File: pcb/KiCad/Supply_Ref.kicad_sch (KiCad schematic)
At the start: 39 parts, among them J9 RF_Shield_One_Piece, U1 LT3045EMSE, U2 LT3094EMSE, U3 LT1236-10, U6 LT8610

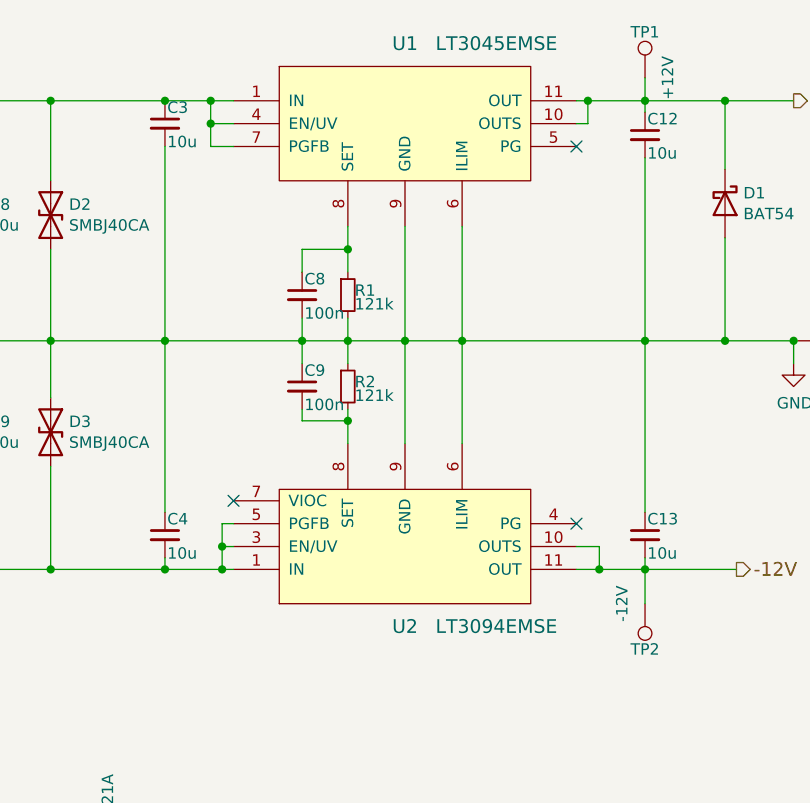
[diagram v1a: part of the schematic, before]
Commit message: Fix custom symbols. Update production files.
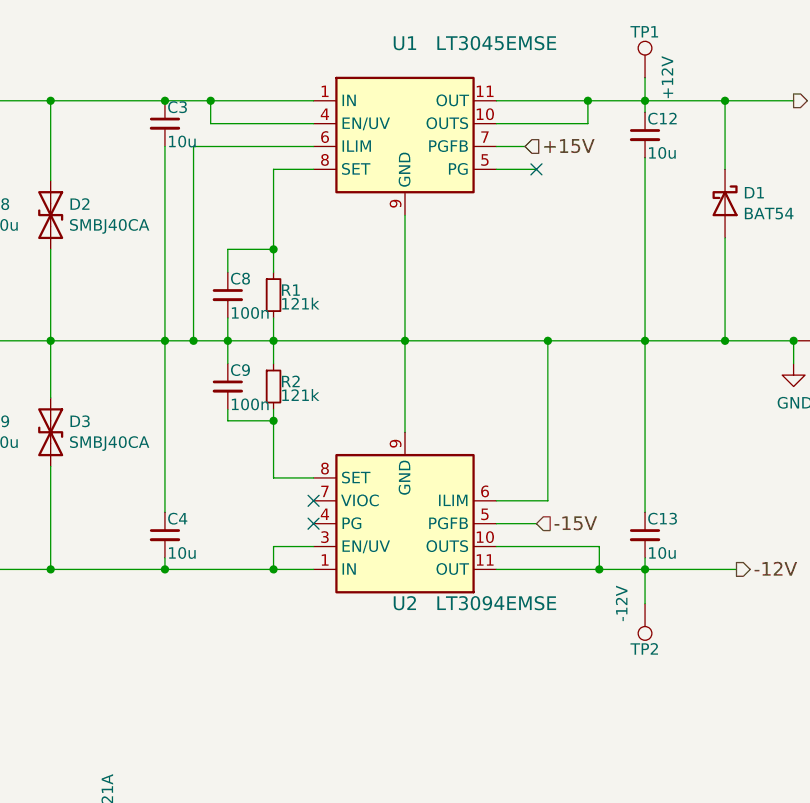
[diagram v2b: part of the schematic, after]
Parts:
- U1: symbol LinearTechnology:LT3045EMSE -> Regulator_Linear:LT3045xMSE; MFN Analog Devices -> Linear Technology; MFP (none) -> LT3045EMSE
- U2: symbol LinearTechnology:LT3094EMSE -> Regulator_Linear:LT3094xMSE
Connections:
- net IN renamed +15V
- now unconnected: U3.1 (NC), U3.3 (NC), U3.7 (NC), U3.8 (NC)
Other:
- moved on the sheet: C8, C9, R1, R2, U2

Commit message: Update BOM
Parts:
- RV1: MFN Vishay -> Molex; PN 534B1103JC -> 22-23-2031
- U1: MFP LT3045EMSE -> (none)
- U2: Alternative LT3094EMSE#PBF -> (none); PN LT3094EMSE#TRPBF -> LT3094EMSE#PBF
- U6: PN LT8610EMSE#TRPBF -> LT8610EMSE#PBF
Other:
- note added: "Connect 10k-trimpot: Vishay 534B1103JC"
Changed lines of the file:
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@@
     (stroke (width 0) (type default) (color 0 0 0 0))
+  )
+  (text "Connect 10k-trimpot:\nVishay 534B1103JC" (at 234.95 50.8 0)
+    (effects (font (size 1.524 1.524)) (justify left bottom))
   )
   (hierarchical_label "+15V" (shape input) (at 33.02 134.62 180)
@@
       (effects (font (size 1.524 1.524)) hide)
     )
-    (property "PN" "LT8610EMSE#TRPBF" (id 5) (at 85.09 172.72 0)
+    (property "PN" "LT8610EMSE#PBF" (id 5) (at 85.09 172.72 0)
       (effects (font (size 1.27 1.27)) hide)
     )
@@
       (effects (font (size 1.27 1.27)) hide)
     )
-    (property "MFP" "LT3045EMSE" (id 6) (at 93.98 54.61 0)
-      (effects (font (size 1.524 1.524)) hide)
-    )
     (pin "1")
     (pin "10")
@@
       (effects (font (size 1.524 1.524)) hide)
     )
-    (property "PN" "LT3094EMSE#TRPBF" (id 5) (at 78.74 86.36 0)
-      (effects (font (size 1.27 1.27)) hide)
-    )
-    (property "Alternative" "LT3094EMSE#PBF" (id 6) (at 78.74 86.36 0)
+    (property "PN" "LT3094EMSE#PBF" (id 5) (at 78.74 86.36 0)
       (effects (font (size 1.27 1.27)) hide)
     )
@@
       (effects (font (size 1.27 1.27)) hide)
     )
-    (property "MFN" "Vishay" (id 4) (at 232.41 43.18 0)
-      (effects (font (size 1.27 1.27)) hide)
-    )
-    (property "PN" "534B1103JC" (id 5) (at 232.41 43.18 0)
-      (effects (font (size 1.27 1.27)) hide)
-    )
+    (property "MFN" "Molex" (id 4) (at 232.41 43.18 0)
+      (effects (font (size 1.27 1.27)) hide)
+    )
+    (property "PN" "22-23-2031" (id 5) (at 232.41 43.18 0)
+      (effects (font (size 1.27 1.27)) hide)
+    )

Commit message: Set symbols and mounting holes to DNF.
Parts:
- TP1, TP2, TP3, TP4, TP5: Config (none) -> DNF
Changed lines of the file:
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@@
       (effects (font (size 1.27 1.27)) hide)
     )
-    (property "Config" "" (id 4) (at 121.92 143.51 0)
+    (property "Config" "DNF" (id 4) (at 121.92 143.51 0)
       (effects (font (size 1.524 1.524)) hide)
     )
@@
       (effects (font (size 1.27 1.27)) hide)
     )
-    (property "Config" "" (id 4) (at 105.41 95.25 0)
+    (property "Config" "DNF" (id 4) (at 105.41 95.25 0)
       (effects (font (size 1.524 1.524)) hide)
     )
@@
       (effects (font (size 1.27 1.27)) hide)
     )
-    (property "Config" "" (id 4) (at 105.41 36.83 0)
+    (property "Config" "DNF" (id 4) (at 105.41 36.83 0)
       (effects (font (size 1.524 1.524)) hide)
     )
@@
       (effects (font (size 1.27 1.27)) hide)
     )
-    (property "Config" "" (id 4) (at 121.92 66.04 0)
+    (property "Config" "DNF" (id 4) (at 121.92 66.04 0)
       (effects (font (size 1.524 1.524)) hide)
     )
@@
       (effects (font (size 1.27 1.27)) hide)
     )
-    (property "Config" "" (id 4) (at 217.17 38.1 0)
+    (property "Config" "DNF" (id 4) (at 217.17 38.1 0)
       (effects (font (size 1.524 1.524)) hide)
     )

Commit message: Fix 'current' output stage.
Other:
- title: RedPitaya Lockbox: +/-12V,+5V Supply and +10V Reference -> RedPitaya Lockbox
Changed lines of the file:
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@@
   (paper "A4")
   (title_block
-    (title "RedPitaya Lockbox: +/-12V,+5V Supply and +10V Reference")
-    (date "2022-02-22")
-    (rev "1.6")
+    (title "RedPitaya Lockbox")
+    (date "2023-08-08")
+    (rev "1.6.1")
     (company "Atoms-Photons-Quanta, Institut für Angewandte Physik, TU Darmstadt")
     (comment 1 "Tilman Preuschoff")

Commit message: Fit RF shield
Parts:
- J9: Config DNF -> (none)
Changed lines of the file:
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@@
       (effects (font (size 1.27 1.27)) hide)
     )
-    (property "Config" "DNF" (id 6) (at 252.73 142.24 0)
+    (property "Config" "" (id 6) (at 252.73 142.24 0)
       (effects (font (size 1.524 1.524)) hide)
     )

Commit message: Add alternative PN for voltage ref.
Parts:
- U3: Alternative (none) -> LT1236CIS8-10#PBF
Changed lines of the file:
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@@
       (effects (font (size 1.27 1.27)) hide)
+    )
+    (property "Alternative" "LT1236CIS8-10#PBF" (id 6) (at 198.12 40.64 0)
+      (effects (font (size 1.524 1.524)) hide)
     )
     (pin "1")

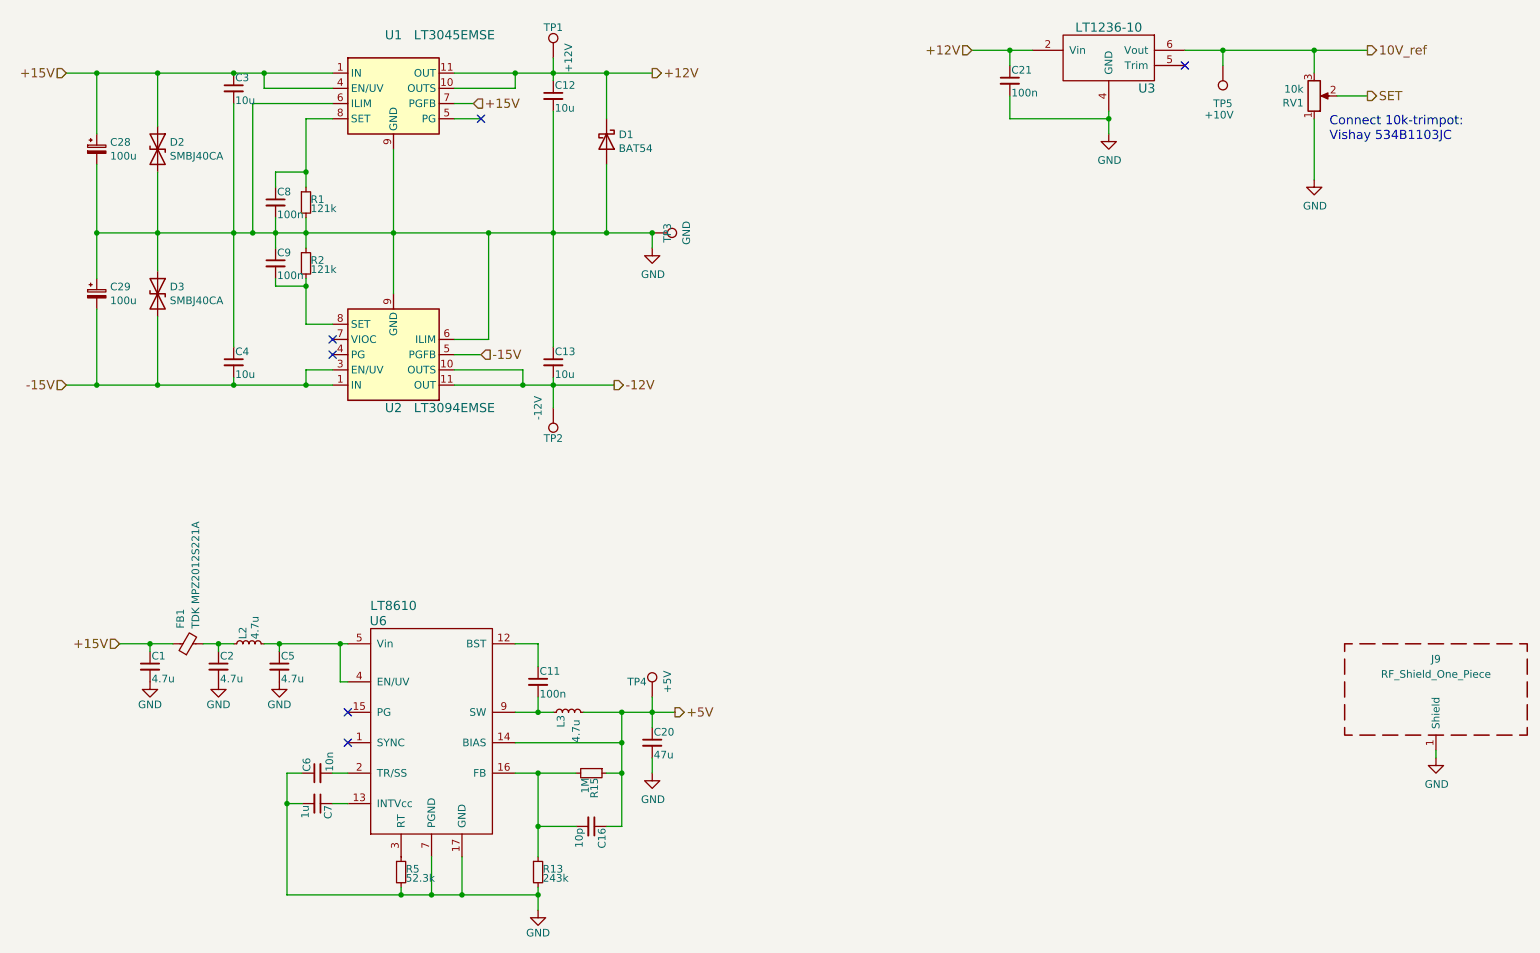
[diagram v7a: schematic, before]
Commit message: Updated to KiCAD 7 Cleaned up schematics Updated footprints Cleaned up PCB
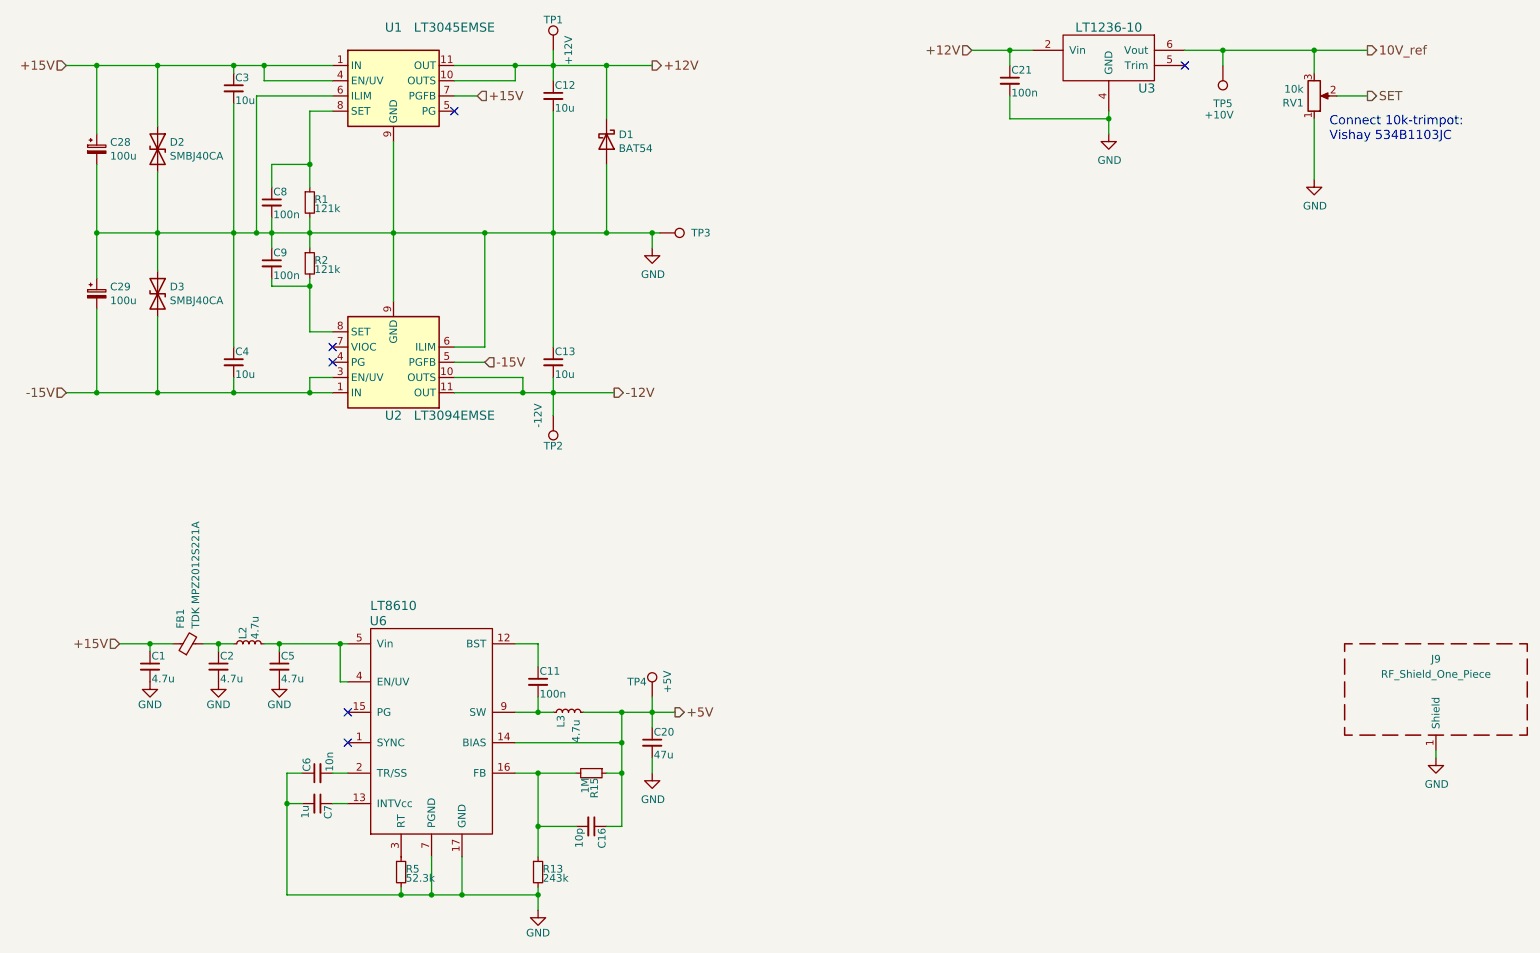
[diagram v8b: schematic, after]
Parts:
- TP3: value GND -> TestPoint
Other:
- moved on the sheet: C8, C9, R1, R2, TP1, TP2, TP3, U1, U2
